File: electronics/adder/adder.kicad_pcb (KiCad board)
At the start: 2 copper layers, 108.6 x 76.2 mm, 0 parts

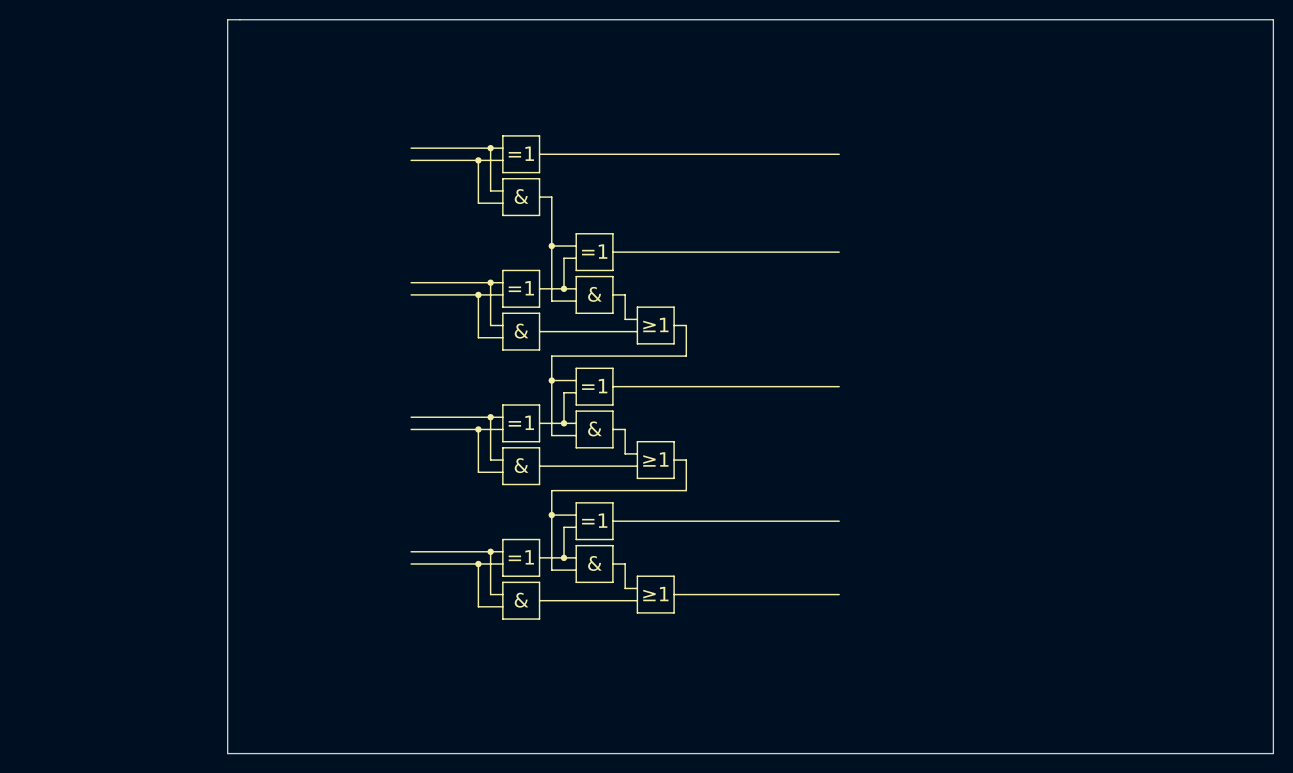
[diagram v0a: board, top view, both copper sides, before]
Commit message: add some parts to pcb
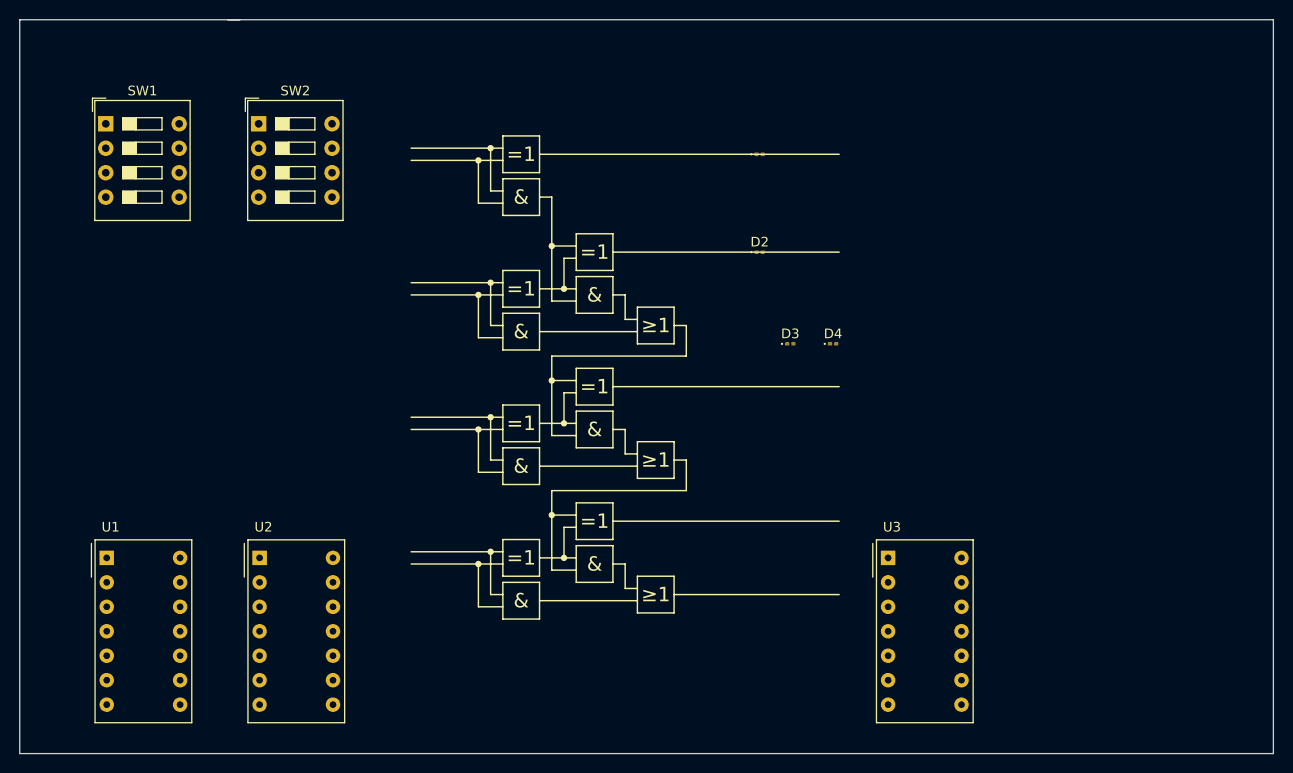
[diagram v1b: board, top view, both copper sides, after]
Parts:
- added D1: LED, Diode_SMD:D_0201_0603Metric, F.Cu at (144.1, 52.1)
- added D2: LED, Diode_SMD:D_0201_0603Metric, F.Cu at (144.1, 62.2)
- added D3: LED, Diode_SMD:D_0201_0603Metric, F.Cu at (147.3, 71.8)
- added D4: LED, Diode_SMD:D_0201_0603Metric, F.Cu at (151.8, 71.8)
- added SW1: SW_DIP_x04, Button_Switch_THT:SW_DIP_SPSTx04_Slide_9.78x12.34mm_W7.62mm_P2.54mm, F.Cu at (76.2, 48.9)
- added SW2: SW_DIP_x04, Button_Switch_THT:SW_DIP_SPSTx04_Slide_9.78x12.34mm_W7.62mm_P2.54mm, F.Cu at (92.1, 48.9)
- added U1: MAN71A, Display_7Segment:MAN71A, F.Cu at (76.3, 94.0)
- added U2: MAN71A, Display_7Segment:MAN71A, F.Cu at (92.2, 94.0)
- added U3: MAN71A, Display_7Segment:MAN71A, F.Cu at (157.5, 94.0)
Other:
- board size 108.6 x 76.2 mm -> 130.2 x 76.2 mm
